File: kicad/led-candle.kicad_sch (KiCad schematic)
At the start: 7 parts

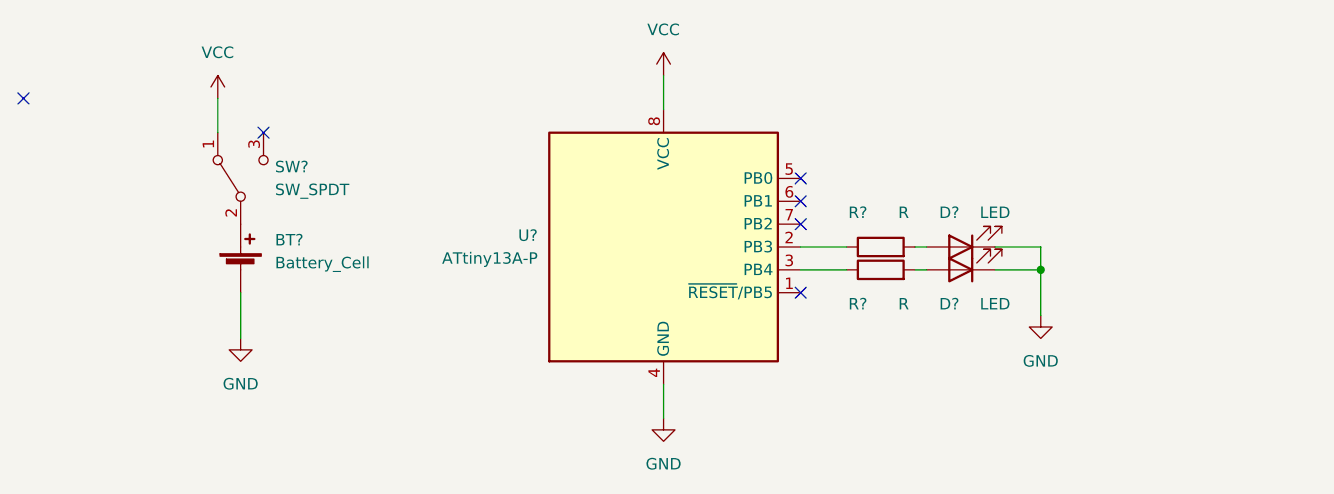
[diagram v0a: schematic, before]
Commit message: feat: add PCB layout, remove optional LED from schematic
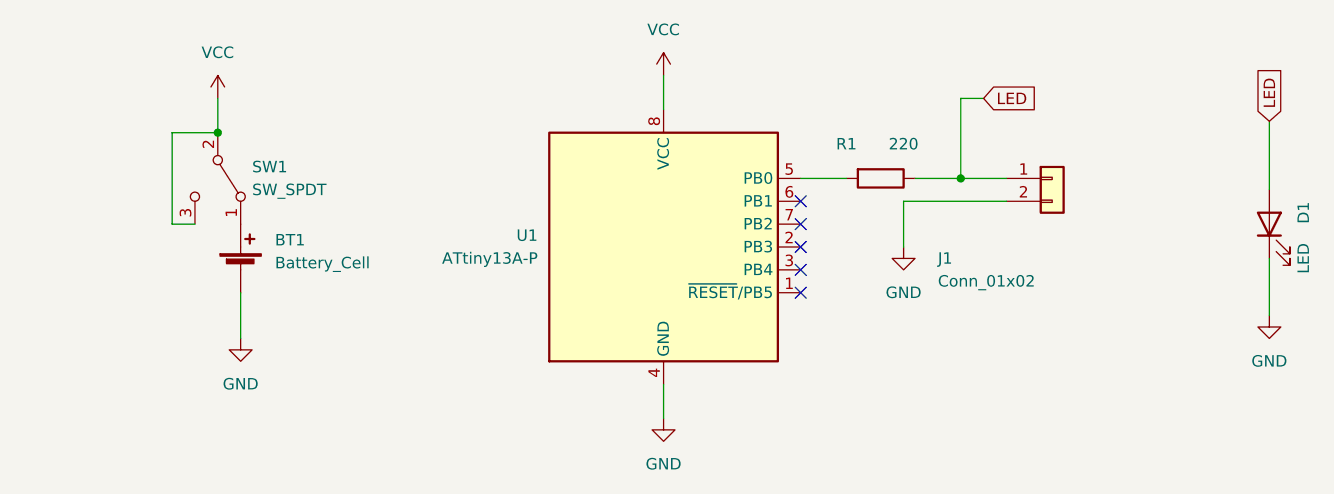
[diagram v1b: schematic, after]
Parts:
- removed D?: LED, symbol Device:LED
- removed R?: R, symbol Device:R
- added J1: Conn_01x02, Connector_PinHeader_2.54mm:PinHeader_1x02_P2.54mm_Vertical, symbol Connector_Generic:Conn_01x02
- D1: renamed from D?; footprint (none) -> LED_THT:LED_D5.0mm
- R1: renamed from R?; value R -> 220; footprint (none) -> Resistor_THT:R_Axial_DIN0207_L6.3mm_D2.5mm_P2.54mm_Vertical
- SW1: renamed from SW?; footprint (none) -> Button_Switch_THT:SW_CuK_JS202011CQN_DPDT_Straight
- gave numbers to parts that had none: 2
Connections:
- net GND: now also J1.2 (Pin_2)
- net VCC: now also SW1.2 (B), SW1.3 (C); no longer SW1.1 (A)
- net at BT1.1 (+): now also SW1.1 (A); no longer SW1.2 (B)
- net at R1.2: now also U1.5 (PB0); no longer D1.2 (A)
- net at U1.2 (PB3): no longer R1.1
- new net LED: D1.2 (A), J1.1 (Pin_1), R1.1
- no-connect marks 6 -> 5
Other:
- moved on the sheet: D1, R1, SW1
